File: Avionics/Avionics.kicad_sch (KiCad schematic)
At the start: 8 parts, among them SW1 SW_SPST, U1 ATmega328P-A, Y1 Crystal_GND24

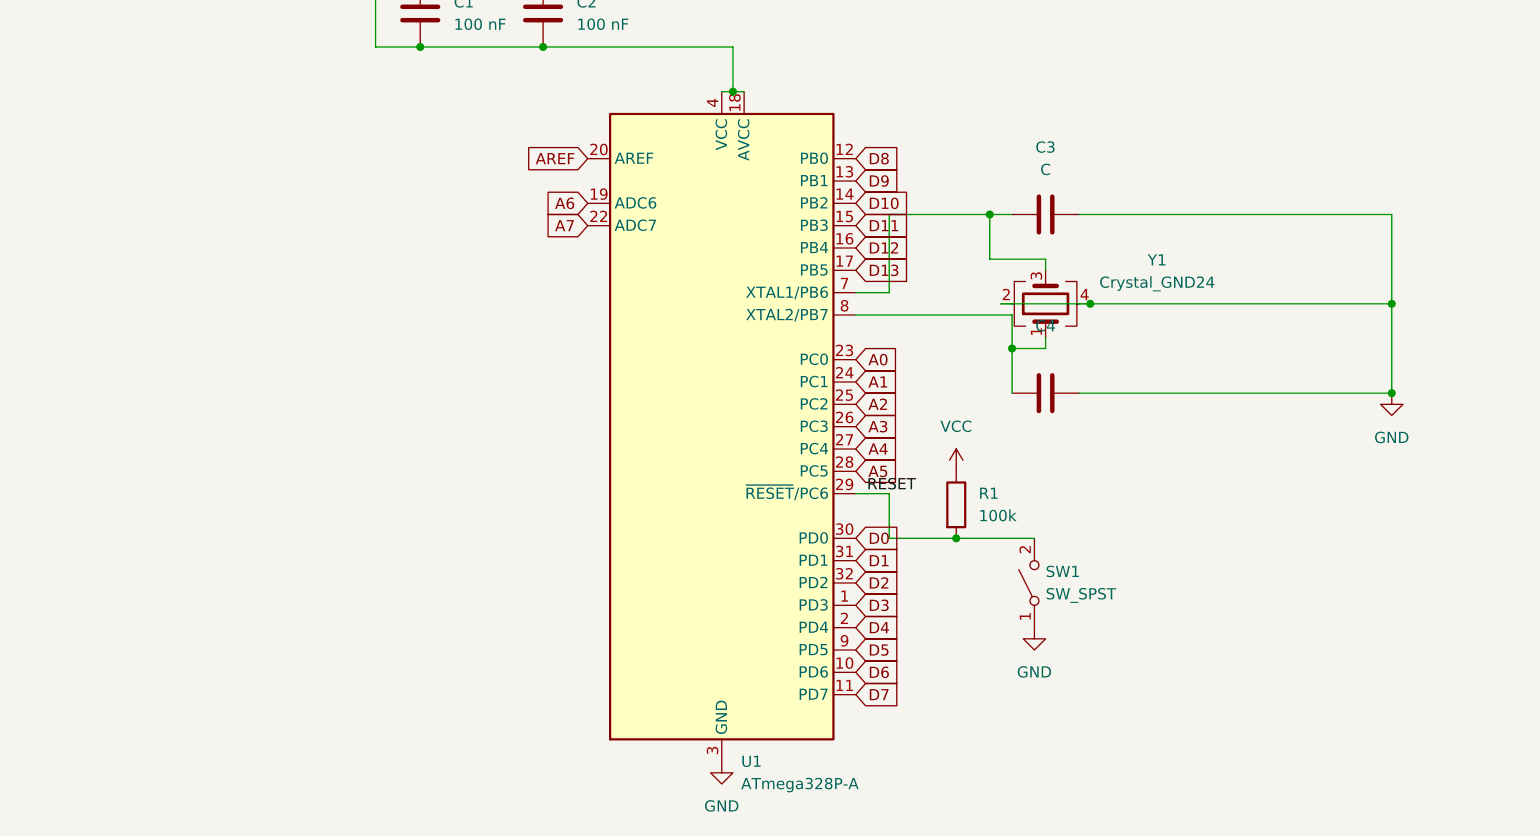
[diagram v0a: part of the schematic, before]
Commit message: Hour 2
Designed PCB from Schematic (I think it works)
Adding accelerometer (Still need to connect it)
Adding LEDs
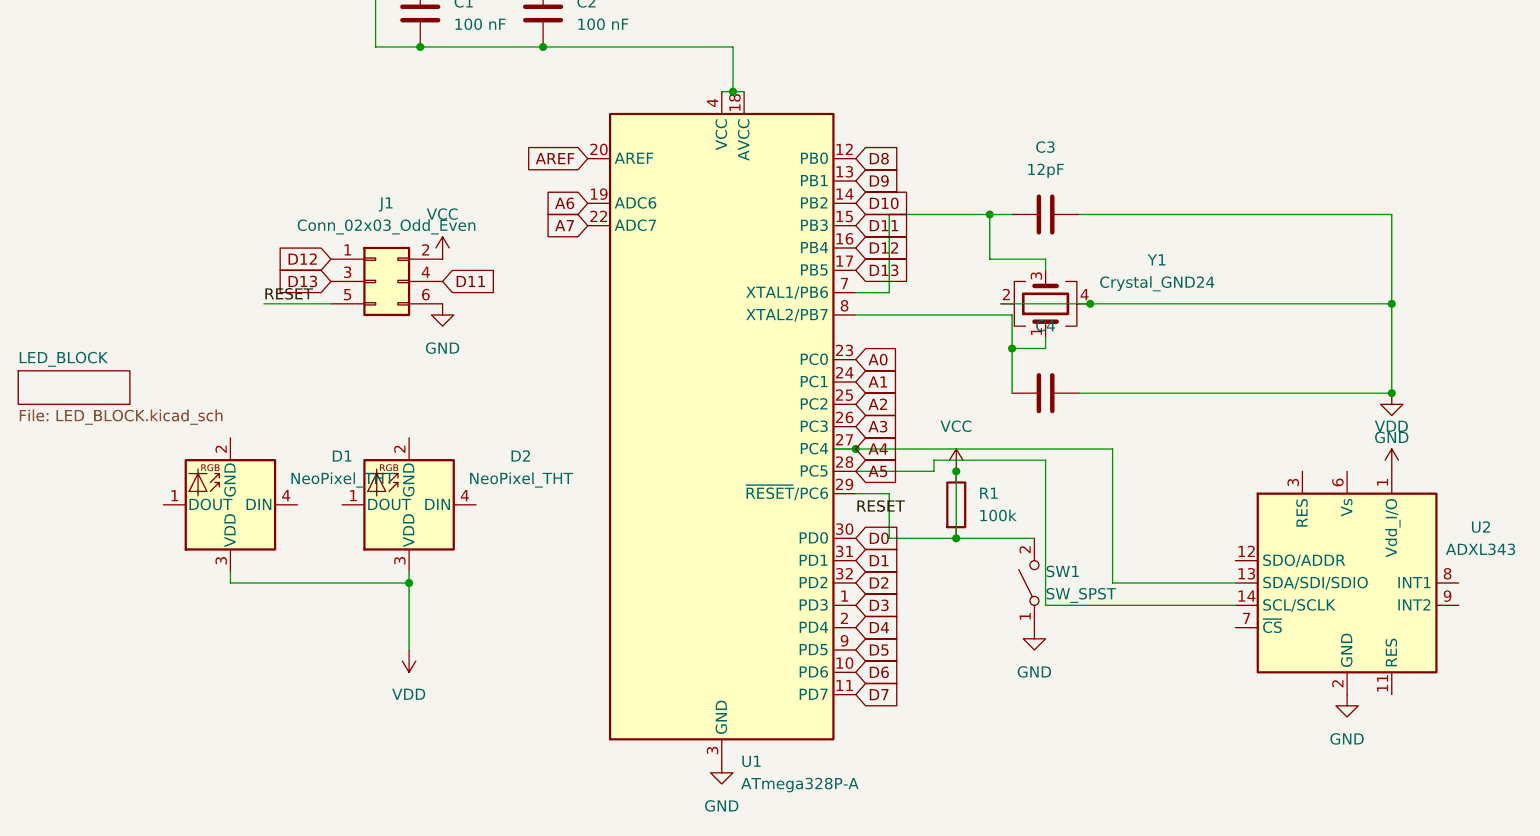
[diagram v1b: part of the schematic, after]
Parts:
- added D1, D2: NeoPixel_THT, symbol LED:NeoPixel_THT
- added J1: Conn_02x03_Odd_Even, Connector_PinHeader_2.54mm:PinHeader_2x03_P2.54mm_Vertical, symbol Connector_Generic:Conn_02x03_Odd_Even
- added U2: ADXL343, Package_LGA:LGA-14_3x5mm_P0.8mm_LayoutBorder1x6y, symbol Sensor_Motion:ADXL343
- C1, C2: footprint (none) -> Capacitor_SMD:C_0805_2012Metric_Pad1.18x1.45mm_HandSolder
- C3, C4: value C -> 12pF; footprint (none) -> Capacitor_SMD:C_0805_2012Metric_Pad1.18x1.45mm_HandSolder
- R1: footprint (none) -> Resistor_SMD:R_0805_2012Metric_Pad1.20x1.40mm_HandSolder
- SW1: footprint (none) -> Button_Switch_SMD:SW_Push_1P1T_XKB_TS-1187A
- Y1: footprint (none) -> Crystal:Crystal_SMD_3225-4Pin_3.2x2.5mm_HandSoldering
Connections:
- net A4: now also U2.13 (SDA/SDI/SDIO)
- net A5: now also U2.14 (SCL/SCLK)
- net D11: now also J1.4 (Pin_4)
- net D12: now also J1.1 (Pin_1)
- net D13: now also J1.3 (Pin_3)
- net GND: now also J1.6 (Pin_6), U2.2 (GND), U2.4 (GND), U2.5 (GND)
- net RESET: now also J1.5 (Pin_5); no longer R1.2, SW1.2 (B), U1.29 (~{RESET}/PC6)
- net VCC: now also R1.2, SW1.2 (B), U1.29 (~{RESET}/PC6), J1.2 (Pin_2)
- new net VDD: D1.3 (VDD), D2.3 (VDD), U2.1 (Vdd_I/O)
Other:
- added sheet LED_BLOCK (LED_BLOCK.kicad_sch)

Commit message: 3hr
very tired
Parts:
- added C5, C6: 100 nF, Capacitor_SMD:C_0805_2012Metric_Pad1.18x1.45mm_HandSolder, symbol Device:C
- added C7: C, Capacitor_SMD:C_0805_2012Metric_Pad1.18x1.45mm_HandSolder, symbol Device:C
- added C8: 1 uF, Capacitor_SMD:C_0805_2012Metric_Pad1.18x1.45mm_HandSolder, symbol Device:C
- added C9: 0.1 uF, Capacitor_SMD:C_0805_2012Metric_Pad1.18x1.45mm_HandSolder, symbol Device:C
- added D10, D11: D, Diode_SMD:D_0201_0603Metric, symbol Device:D
- added D3, D4, D5, D6, D7, D8: NeoPixel_THT, LED_SMD:LED_WS2812_PLCC6_5.0x5.0mm_P1.6mm, symbol LED:NeoPixel_THT
- added D9: C35722, Diode_SMD:D_0201_0603Metric, symbol Device:D
- added J2: USB_C_Receptacle_USB2.0_16P, Connector_USB:USB_C_Receptacle_Amphenol_12401548E4-2A, symbol Connector:USB_C_Receptacle_USB2.0_16P
- added R2, R3: 5k1, Resistor_SMD:R_0805_2012Metric_Pad1.20x1.40mm_HandSolder, symbol Device:R
- added R4, R5: 1k, Resistor_SMD:R_0805_2012Metric_Pad1.20x1.40mm_HandSolder, symbol Device:R
- added R6: 10k, Resistor_SMD:R_0805_2012Metric_Pad1.20x1.40mm_HandSolder, symbol Device:R
- added U3: CH340N, Package_SO:SOP-8_3.9x4.9mm_P1.27mm, symbol Interface_USB:CH340N
- D1, D2: footprint (none) -> LED_SMD:LED_WS2812_PLCC6_5.0x5.0mm_P1.6mm
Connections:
- net D0: now also D11.1 (K), U3.6 (TXD)
- net D1: now also D10.1 (K), U3.7 (RXD)
- net D2: now also D3.4 (DIN)
- net D3: now also D4.4 (DIN)
- net D4: now also D5.4 (DIN)
- net D5: now also D6.4 (DIN)
- net D6: now also D7.4 (DIN)
- net D7: now also D8.4 (DIN)
- net GND: now also D1.2 (GND), D2.2 (GND), C5.1, C6.2, C8.1, C9.2, D3.2 (GND), D4.2 (GND), D5.2 (GND), D6.2 (GND), D7.2 (GND), D8.2 (GND), J2.A1 (GND), J2.A12 (GND), J2.B1 (GND), J2.B12 (GND), R2.2, R3.1, U3.3 (GND)
- net RESET: now also C7.2
- net VCC: now also D9.1 (K), R6.2
- net VDD: now also C9.1; no longer D1.3 (VDD), D2.3 (VDD)
- net at U2.7 (~{CS}): now also R6.1
- new net: D10.2 (A), R5.2
- new net: C6.1, R4.1, R5.1, U3.5 (VCC)
- new net: C5.2, U3.8 (V3)
- new net: J2.B5 (CC2), R3.2
- new net: J2.A5 (CC1), R2.1
- new net: C7.1, U3.4 (~{RTS})
- new net: D11.2 (A), R4.2
- new net UD+: J2.A6 (D+), J2.B6 (D+), U3.1 (UD+)
- new net UD-: J2.A7 (D-), J2.B7 (D-), U3.2 (UD-)
- new net VBUS: D9.2 (A), J2.A4 (VBUS), J2.A9 (VBUS), J2.B4 (VBUS), J2.B9 (VBUS)
- new net VS: C8.2
- no-connect marks 0 -> 7
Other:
- removed sheet LED_BLOCK

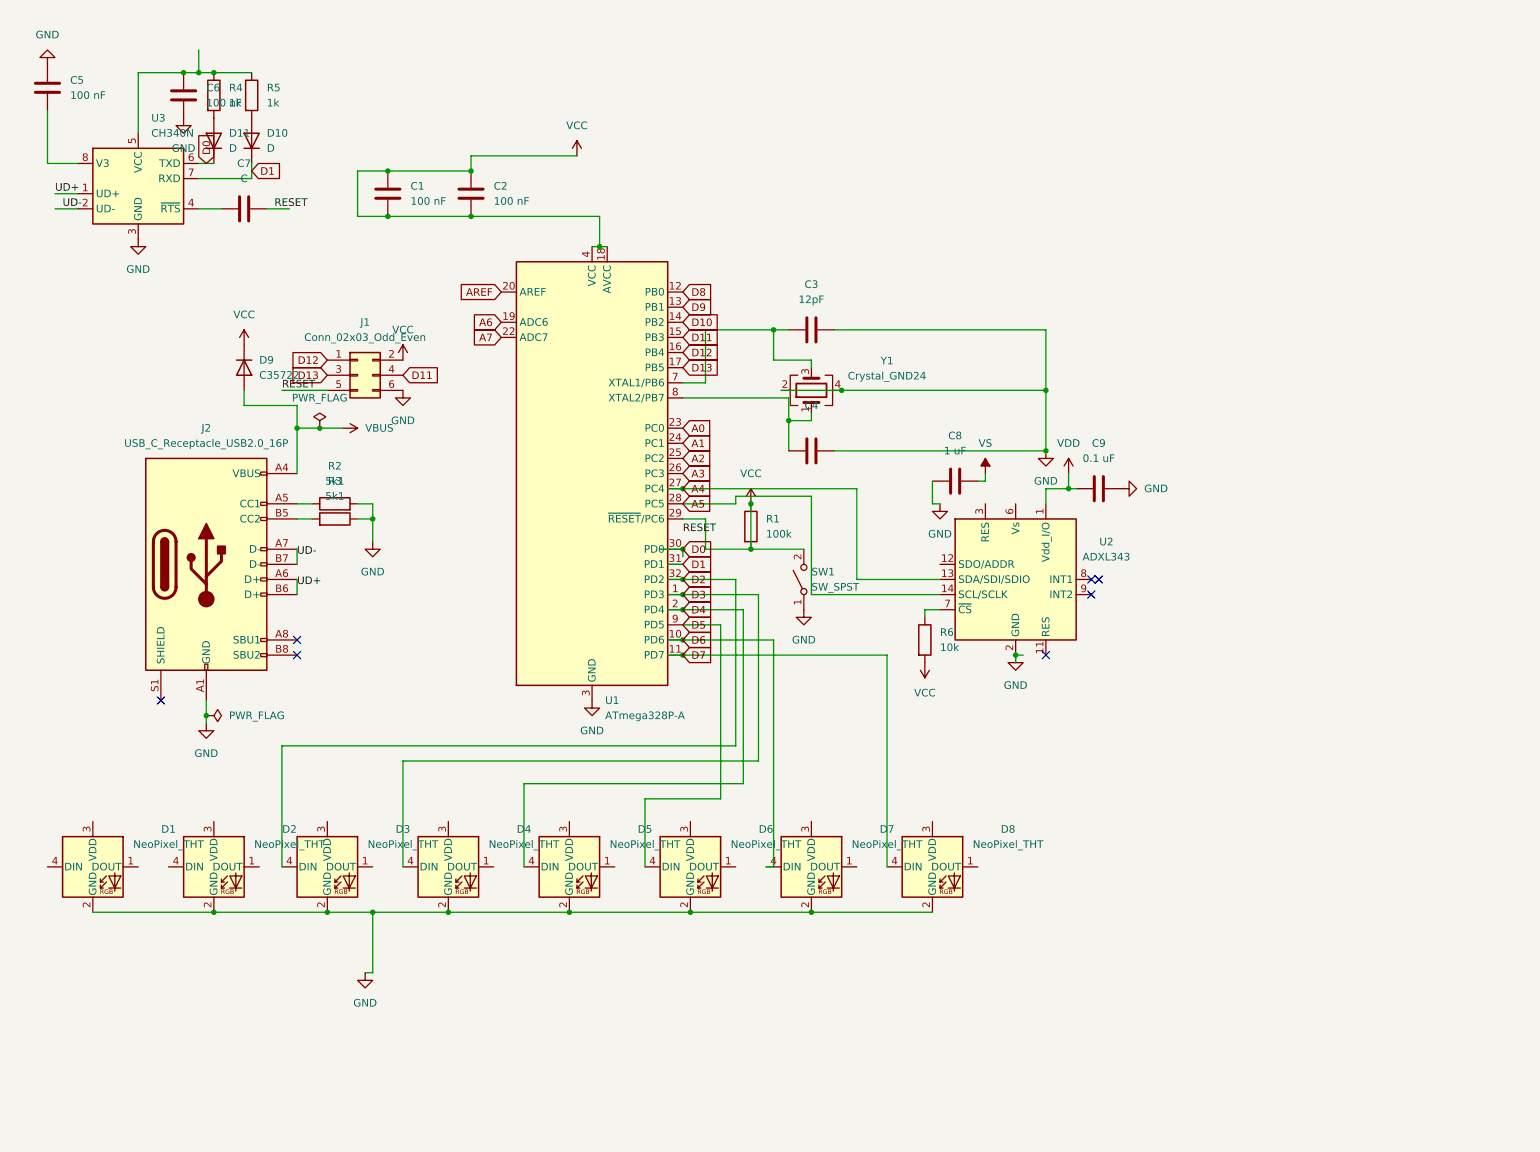
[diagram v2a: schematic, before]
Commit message: 3 hr
Added barometer / altimeter, battery, arduino pinout
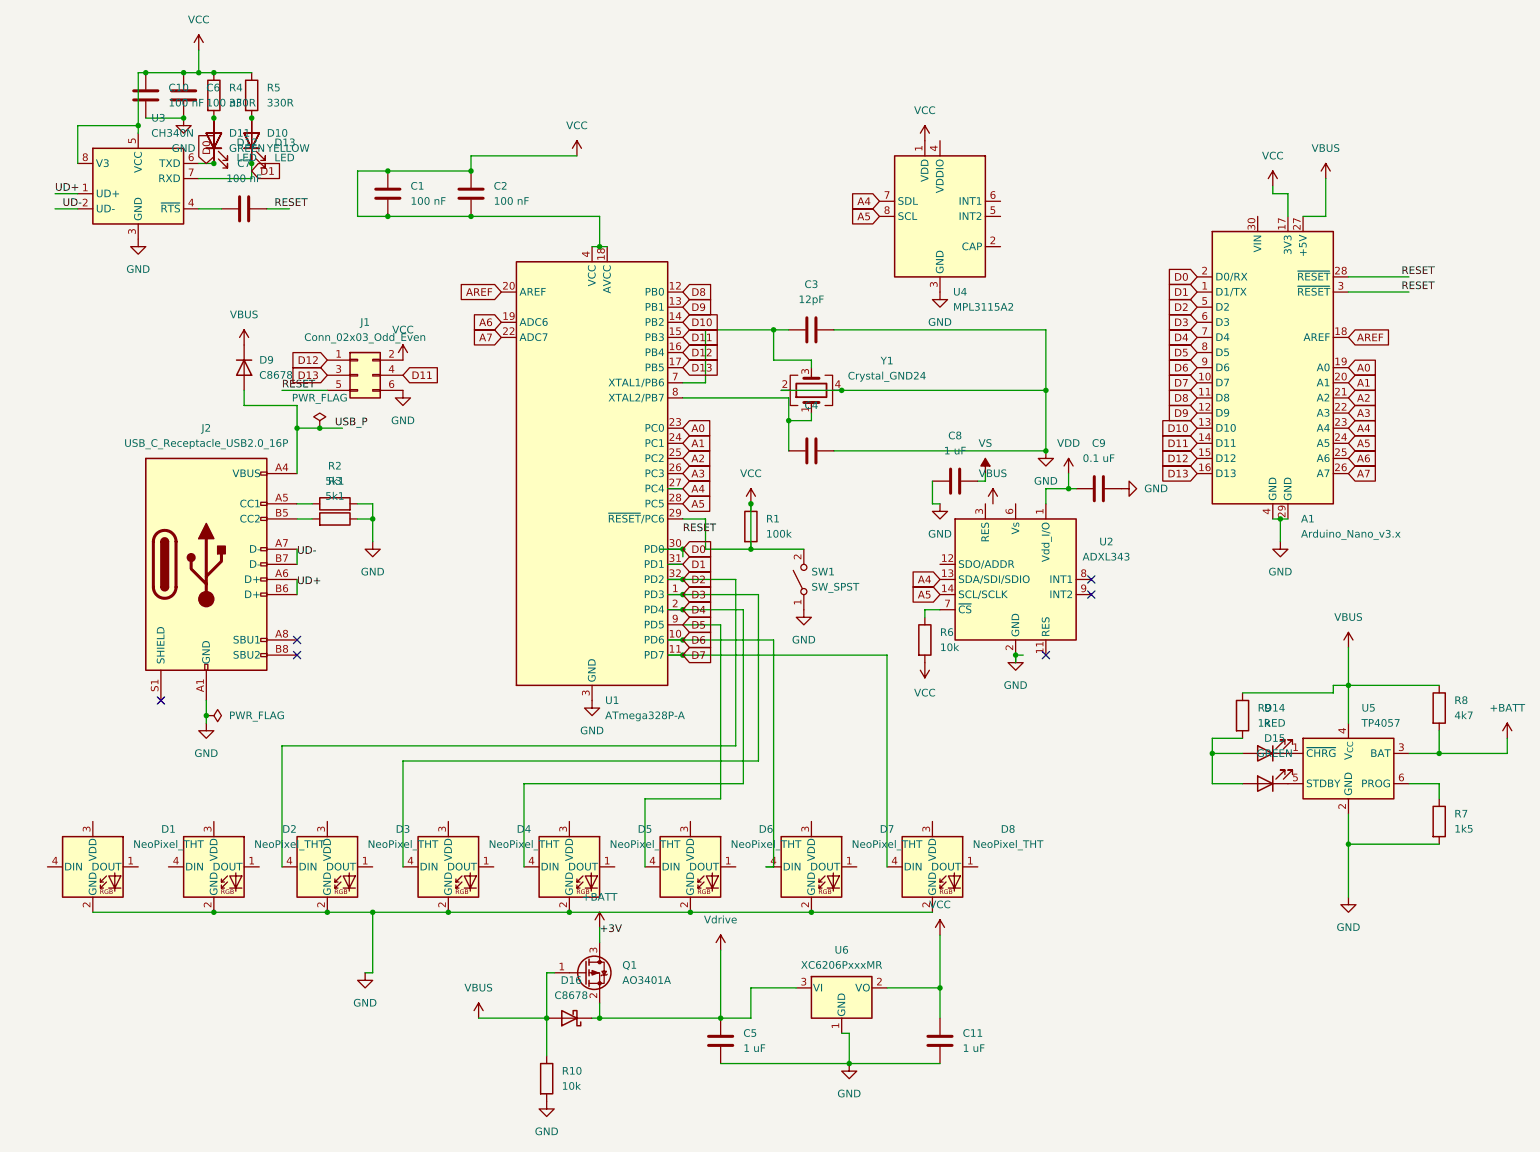
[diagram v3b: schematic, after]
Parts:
- added A1: Arduino_Nano_v3.x, Module:Arduino_Nano_WithMountingHoles, symbol MCU_Module:Arduino_Nano_v3.x
- added C10: 100 nF, Capacitor_SMD:C_0805_2012Metric_Pad1.18x1.45mm_HandSolder, symbol Device:C
- added C11: 1 uF, Capacitor_SMD:C_0805_2012Metric_Pad1.18x1.45mm_HandSolder, symbol Device:C
- added D12, D13: LED, Diode_SMD:D_1206_3216Metric_Pad1.42x1.75mm_HandSolder, symbol Device:LED
- added D14: RED, Diode_SMD:D_1206_3216Metric_Pad1.42x1.75mm_HandSolder, symbol Device:LED
- added D15: GREEN, Diode_SMD:D_1206_3216Metric_Pad1.42x1.75mm_HandSolder, symbol Device:LED
- added D16: C8678, Diode_SMD:D_1206_3216Metric, symbol Device:D_Schottky
- added Q1: AO3401A, Package_TO_SOT_SMD:SOT-23, symbol Transistor_FET:AO3401A
- added R10: 10k, Resistor_SMD:R_0805_2012Metric_Pad1.20x1.40mm_HandSolder, symbol Device:R
- added R7: 1k5, Resistor_SMD:R_0805_2012Metric_Pad1.20x1.40mm_HandSolder, symbol Device:R
- added R8: 4k7, Resistor_SMD:R_0805_2012Metric_Pad1.20x1.40mm_HandSolder, symbol Device:R
- added R9: 1k, Resistor_SMD:R_0805_2012Metric_Pad1.20x1.40mm_HandSolder, symbol Device:R
- added U4: MPL3115A2, Package_LGA:NXP_LGA-8_3x5mm_P1.25mm_H1.1mm, symbol Sensor_Pressure:MPL3115A2
- added U5: TP4057, Package_TO_SOT_SMD:TSOT-23-5, symbol Battery_Management:TP4057
- added U6: XC6206PxxxMR, Package_TO_SOT_SMD:SOT-23-3, symbol Regulator_Linear:XC6206PxxxMR
- C5: value 100 nF -> 1 uF
- C7: value C -> 100 nF
- D10: value D -> YELLOW; footprint Diode_SMD:D_0201_0603Metric -> Diode_SMD:D_SMC_Handsoldering
- D11: value D -> GREEN; footprint Diode_SMD:D_0201_0603Metric -> Diode_SMD:D_SMC_Handsoldering
- D9: value C35722 -> C8678; footprint Diode_SMD:D_0201_0603Metric -> Diode_SMD:D_SMC_Handsoldering
- R4, R5: value 1k -> 330R
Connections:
- net A0: now also A1.19 (A0)
- net A1: now also A1.20 (A1)
- net A2: now also A1.21 (A2)
- net A3: now also A1.22 (A3)
- net A4: now also A1.23 (A4), U4.7 (SDL)
- net A5: now also A1.24 (A5), U4.8 (SCL)
- net A6: now also A1.25 (A6)
- net A7: now also A1.26 (A7)
- net AREF: now also A1.18 (AREF)
- net D0: now also A1.2 (D0/RX), D12.1 (K)
- net D1: now also A1.1 (D1/TX), D13.1 (K)
- net D10: now also A1.13 (D10)
- net D11: now also A1.14 (D11)
- net D12: now also A1.15 (D12)
- net D13: now also A1.16 (D13)
- net D2: now also A1.5 (D2)
- net D3: now also A1.6 (D3)
- net D4: now also A1.7 (D4)
- net D5: now also A1.8 (D5)
- net D6: now also A1.9 (D6)
- net D7: now also A1.10 (D7)
- net D8: now also A1.11 (D8)
- net D9: now also A1.12 (D9)
- net GND: now also C5.2, A1.29 (GND), A1.4 (GND), C10.2, C11.2, R10.2, R7.2, U4.3 (GND), U5.2 (GND), U6.1 (GND); no longer C5.1
- net RESET: now also A1.28 (~{RESET}), A1.3 (~{RESET})
- net VBUS: now also D9.1 (K), A1.27 (+5V), D16.2 (A), Q1.1 (G), R10.1, R8.1, R9.1, U5.4 (V_{CC}); no longer D9.2 (A), J2.A4 (VBUS), J2.A9 (VBUS), J2.B4 (VBUS), J2.B9 (VBUS)
- net VCC: now also C6.1, R4.1, R5.1, U3.5 (VCC), U3.8 (V3), A1.17 (3V3), C10.1, C11.1, U4.1 (VDD), U6.2 (VO); no longer D9.1 (K)
- net at D10.2 (A), R5.2: now also D13.2 (A)
- net at D11.2 (A), R4.2: now also D12.2 (A)
- new net: D15.1 (K), U5.5 (STDBY)
- new net: D14.2 (A), D15.2 (A), R9.2
- new net: D14.1 (K), U5.1 (~{CHRG})
- new net: R7.1, U5.6 (PROG)
- new net +BATT: Q1.3 (D), R8.2, U5.3 (BAT)
- new net USB_P: D9.2 (A), J2.A4 (VBUS), J2.A9 (VBUS), J2.B4 (VBUS), J2.B9 (VBUS)
- new net Vdrive: C5.1, D16.1 (K), Q1.2 (S), U6.3 (VI)
- no-connect marks 7 -> 6

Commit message: Another hour
Finished up the schematic (at least I hope) & started working (~ 1/2 way done), with the actual PCB layout.
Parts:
- added R11, R12: 4.7k, Resistor_SMD:R_0805_2012Metric_Pad1.20x1.40mm_HandSolder, symbol Device:R
- added R13, R14: 1k, Resistor_SMD:R_0805_2012Metric_Pad1.20x1.40mm_HandSolder, symbol Device:R
- D16: footprint Diode_SMD:D_1206_3216Metric -> Diode_SMD:D_SMA
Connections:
- net A4: now also R11.2, R14.2
- net A5: now also R12.1, R13.2
- net D1: now also D2.4 (DIN)
- net D8: now also D1.4 (DIN)
- net VCC: now also R11.1, R12.2, R13.1, R14.1
